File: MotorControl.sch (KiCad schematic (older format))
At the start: 2 parts, among them U3 74LVC125

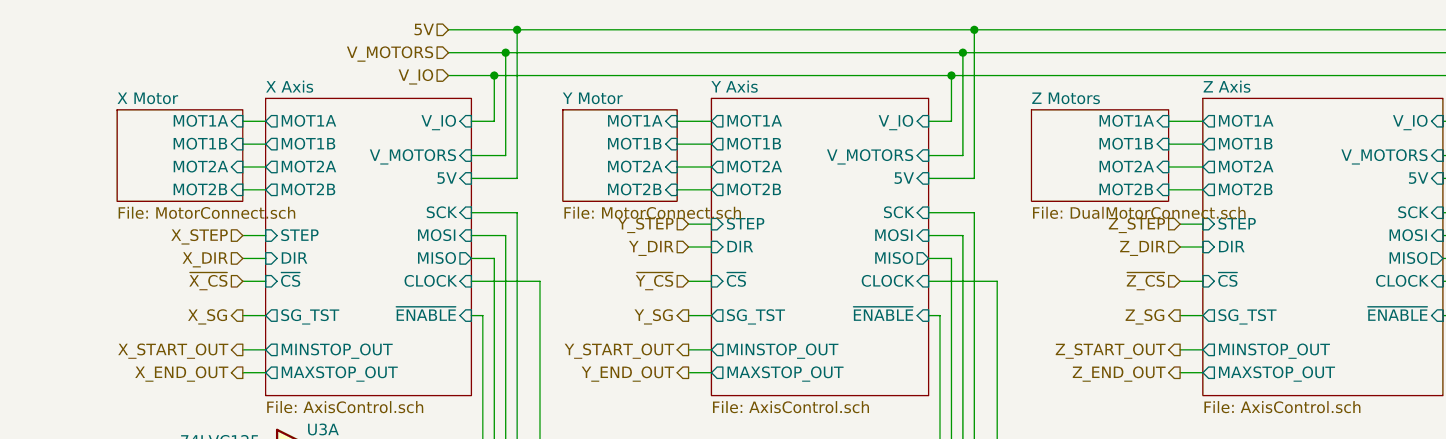
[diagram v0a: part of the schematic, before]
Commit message: Updated motor connector pinout.
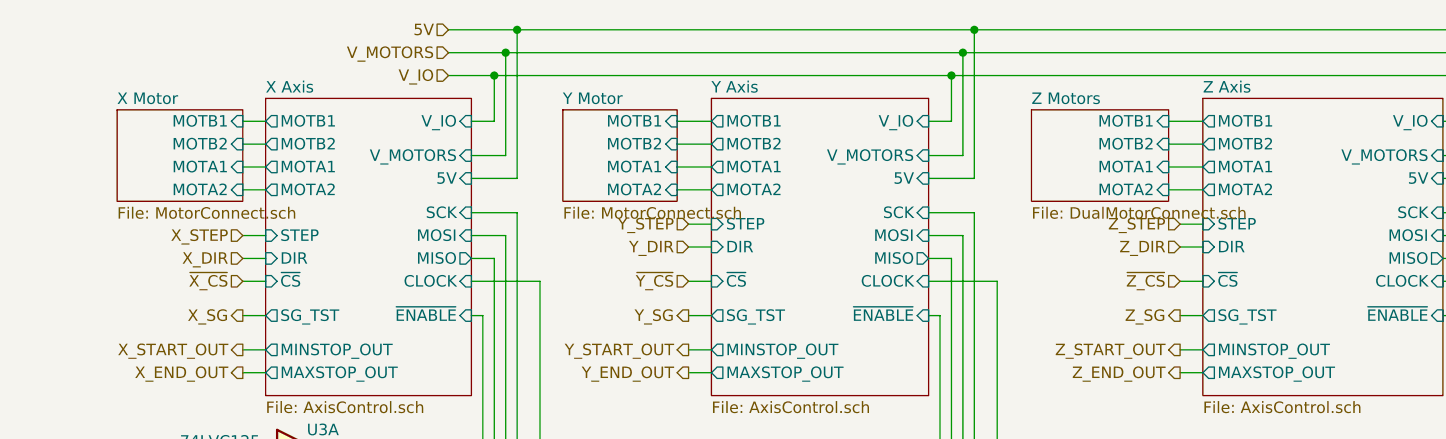
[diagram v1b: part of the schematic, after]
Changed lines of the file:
@@
 F0 "X Axis" 50
 F1 "AxisControl.sch" 50
-F2 "MOT1A" O L 3400 1400 50
-F3 "MOT1B" O L 3400 1500 50
-F4 "MOT2A" O L 3400 1600 50
-F5 "MOT2B" O L 3400 1700 50
-F6 "STEP" I L 3400 1900 50
-F7 "DIR" I L 3400 2000 50
-F8 "~CS" I L 3400 2100 50
-F9 "SG_TST" O L 3400 2250 50
-F10 "V_IO" I R 4300 1400 50
-F11 "V_MOTORS" I R 4300 1550 50
-F12 "SCK" I R 4300 1800 50
-F13 "MOSI" I R 4300 1900 50
-F14 "MISO" O R 4300 2000 50
-F15 "~ENABLE" I R 4300 2250 50
-F16 "MAXSTOP_OUT" O L 3400 2500 50
-F17 "MINSTOP_OUT" O L 3400 2400 50
-F18 "5V" I R 4300 1650 50
-F19 "CLOCK" I R 4300 2100 50
+F2 "STEP" I L 3400 1900 50
+F3 "DIR" I L 3400 2000 50
+F4 "~CS" I L 3400 2100 50
+F5 "SG_TST" O L 3400 2250 50
+F6 "V_IO" I R 4300 1400 50
+F7 "V_MOTORS" I R 4300 1550 50
+F8 "SCK" I R 4300 1800 50
+F9 "MOSI" I R 4300 1900 50
+F10 "MISO" O R 4300 2000 50
+F11 "~ENABLE" I R 4300 2250 50
+F12 "MAXSTOP_OUT" O L 3400 2500 50
+F13 "MINSTOP_OUT" O L 3400 2400 50
+F14 "5V" I R 4300 1650 50
+F15 "CLOCK" I R 4300 2100 50
+F16 "MOTA1" O L 3400 1600 50
+F17 "MOTB1" O L 3400 1400 50
+F18 "MOTA2" O L 3400 1700 50
+F19 "MOTB2" O L 3400 1500 50
 $EndSheet
 $Sheet
@@
 F0 "Y Axis" 50
 F1 "AxisControl.sch" 50
-F2 "MOT1A" O L 5350 1400 50
-F3 "MOT1B" O L 5350 1500 50
-F4 "MOT2A" O L 5350 1600 50
-F5 "MOT2B" O L 5350 1700 50
-F6 "STEP" I L 5350 1850 50
-F7 "DIR" I L 5350 1950 50
-F8 "~CS" I L 5350 2100 50
-F9 "SG_TST" O L 5350 2250 50
-F10 "V_IO" I R 6300 1400 50
-F11 "V_MOTORS" I R 6300 1550 50
-F12 "SCK" I R 6300 1800 50
-F13 "MOSI" I R 6300 1900 50
-F14 "MISO" O R 6300 2000 50
-F15 "~ENABLE" I R 6300 2250 50
-F16 "MAXSTOP_OUT" O L 5350 2500 50
-F17 "MINSTOP_OUT" O L 5350 2400 50
-F18 "5V" I R 6300 1650 50
-F19 "CLOCK" I R 6300 2100 50
+F2 "STEP" I L 5350 1850 50
+F3 "DIR" I L 5350 1950 50
+F4 "~CS" I L 5350 2100 50
+F5 "SG_TST" O L 5350 2250 50
+F6 "V_IO" I R 6300 1400 50
+F7 "V_MOTORS" I R 6300 1550 50
+F8 "SCK" I R 6300 1800 50
+F9 "MOSI" I R 6300 1900 50
+F10 "MISO" O R 6300 2000 50
+F11 "~ENABLE" I R 6300 2250 50
+F12 "MAXSTOP_OUT" O L 5350 2500 50
+F13 "MINSTOP_OUT" O L 5350 2400 50
+F14 "5V" I R 6300 1650 50
+F15 "CLOCK" I R 6300 2100 50
+F16 "MOTA1" O L 5350 1600 50
+F17 "MOTB1" O L 5350 1400 50
+F18 "MOTA2" O L 5350 1700 50
+F19 "MOTB2" O L 5350 1500 50
 $EndSheet
 Wire Wire Line
@@
 F0 "Z Axis" 50
 F1 "AxisControl.sch" 50
-F2 "MOT1A" O L 7500 1400 50
-F3 "MOT1B" O L 7500 1500 50
-F4 "MOT2A" O L 7500 1600 50
-F5 "MOT2B" O L 7500 1700 50
-F6 "STEP" I L 7500 1850 50
-F7 "DIR" I L 7500 1950 50
-F8 "~CS" I L 7500 2100 50
-F9 "SG_TST" O L 7500 2250 50
-F10 "V_IO" I R 8550 1400 50
-F11 "V_MOTORS" I R 8550 1550 50
-F12 "SCK" I R 8550 1800 50
-F13 "MOSI" I R 8550 1900 50
-F14 "MISO" O R 8550 2000 50
-F15 "~ENABLE" I R 8550 2250 50
-F16 "MAXSTOP_OUT" O L 7500 2500 50
-F17 "MINSTOP_OUT" O L 7500 2400 50
-F18 "5V" I R 8550 1650 50
-F19 "CLOCK" I R 8550 2100 50
+F2 "STEP" I L 7500 1850 50
+F3 "DIR" I L 7500 1950 50
+F4 "~CS" I L 7500 2100 50
+F5 "SG_TST" O L 7500 2250 50
+F6 "V_IO" I R 8550 1400 50
+F7 "V_MOTORS" I R 8550 1550 50
+F8 "SCK" I R 8550 1800 50
+F9 "MOSI" I R 8550 1900 50
+F10 "MISO" O R 8550 2000 50
+F11 "~ENABLE" I R 8550 2250 50
+F12 "MAXSTOP_OUT" O L 7500 2500 50
+F13 "MINSTOP_OUT" O L 7500 2400 50
+F14 "5V" I R 8550 1650 50
+F15 "CLOCK" I R 8550 2100 50
+F16 "MOTA1" O L 7500 1600 50
+F17 "MOTB1" O L 7500 1400 50
+F18 "MOTA2" O L 7500 1700 50
+F19 "MOTB2" O L 7500 1500 50
 $EndSheet
 Wire Wire Line
@@
 F0 "X Motor" 50
 F1 "MotorConnect.sch" 50
-F2 "MOT1B" I R 3300 1500 50
-F3 "MOT1A" I R 3300 1400 50
-F4 "MOT2A" I R 3300 1600 50
-F5 "MOT2B" I R 3300 1700 50
+F2 "MOTB1" I R 3300 1400 50
+F3 "MOTB2" I R 3300 1500 50
+F4 "MOTA2" I R 3300 1700 50
+F5 "MOTA1" I R 3300 1600 50
 $EndSheet
 Wire Wire Line
@@
 F0 "Y Motor" 50
 F1 "MotorConnect.sch" 50
-F2 "MOT1B" I R 5200 1500 50
-F3 "MOT1A" I R 5200 1400 50
-F4 "MOT2A" I R 5200 1600 50
-F5 "MOT2B" I R 5200 1700 50
+F2 "MOTB1" I R 5200 1400 50
+F3 "MOTB2" I R 5200 1500 50
+F4 "MOTA2" I R 5200 1700 50
+F5 "MOTA1" I R 5200 1600 50
 $EndSheet
 Wire Wire Line
@@
 F0 "Z Motors" 50
 F1 "DualMotorConnect.sch" 50
-F2 "MOT1A" I R 7350 1400 50
-F3 "MOT1B" I R 7350 1500 50
-F4 "MOT2A" I R 7350 1600 50
-F5 "MOT2B" I R 7350 1700 50
-$EndSheet
-Wire Wire Line
+F2 "MOTB2" I R 7350 1500 50
+F3 "MOTB1" I R 7350 1400 50
+F4 "MOTA2" I R 7350 1700 50
+F5 "MOTA1" I R 7350 1600 50
+$EndSheet
+Wire Wire Line

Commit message: Some useless changes, I'll remove the SD_MODE wire soon.
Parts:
- added JP10: Motor Clock Enable, Jumper:SolderJumper-2_P1.3mm_Open_Pad1.0x1.5mm, symbol Device:Jumper
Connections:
- net labels added: SD_MODE
- wire segments 203 -> 218
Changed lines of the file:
@@
 F16 "5V" I R 4250 4400 50
 F17 "CLOCK" I R 4250 4850 50
+F18 "SD_MODE" I R 4250 5050 50
 $EndSheet
 $Sheet
@@
 F18 "MOTA2" O L 3400 1700 50
 F19 "MOTB2" O L 3400 1500 50
+F20 "SD_MODE" I R 4300 2350 50
 $EndSheet
 $Sheet
@@
 F18 "MOTA2" O L 5350 1700 50
 F19 "MOTB2" O L 5350 1500 50
+F20 "SD_MODE" I R 6300 2350 50
 $EndSheet
 Wire Wire Line
@@
 F18 "MOTA2" O L 7500 1700 50
 F19 "MOTB2" O L 7500 1500 50
+F20 "SD_MODE" I R 8550 2350 50
 $EndSheet
 Wire Wire Line
@@
 F16 "5V" I R 6450 4400 50
 F17 "CLOCK" I R 6450 4850 50
+F18 "SD_MODE" I R 6450 5050 50
 $EndSheet
 Wire Wire Line
@@
 	8550 2100 8800 2100
 Wire Wire Line
-	8800 2100 8800 3250
-Wire Wire Line
 	8800 3450 7300 3450
 Connection ~ 6600 3450
@@
 Wire Wire Line
 	7300 3450 6600 3450
-Wire Wire Line
-	9800 3250 8800 3250
-Connection ~ 8800 3250
-Wire Wire Line
-	8800 3250 8800 3450
 Text HLabel 10550 3250 2    50   Input ~ 0
 CLOCK
 Wire Wire Line
 	10550 3250 10400 3250
+Wire Wire Line
+	8800 2100 8800 3250
+$Comp
+L Device:Jumper JP10
+U 1 1 5AF71511
+P 9100 3250
+F 0 "JP10" H 9100 3514 50  0000 C CNN
+F 1 "Motor Clock Enable" H 9200 3400 50  0000 C CNN
+F 2 "Jumper:SolderJumper-2_P1.3mm_Open_Pad1.0x1.5mm" H 9100 3250 50  0001 C CNN
+F 3 "~" H 9100 3250 50  0001 C CNN
+	1    9100 3250
+	1    0    0    -1
+$EndComp
+Connection ~ 8800 3250
+Wire Wire Line
+	8800 3250 8800 3450
+Wire Wire Line
+	9400 3250 9800 3250
+Wire Wire Line
+	4300 2350 4650 2350
+Wire Wire Line
+	4650 2350 4650 2800
+Wire Wire Line
+	4650 2800 4800 2800
+Wire Wire Line
+	8850 2800 8850 2350
+Wire Wire Line
+	8850 2350 8550 2350
+Wire Wire Line
+	6300 2350 6800 2350
+Wire Wire Line
+	6800 2350 6800 2800
+Connection ~ 6800 2800
+Wire Wire Line
+	6800 2800 7000 2800
+Wire Wire Line
+	6450 5050 7000 5050
+Wire Wire Line
+	7000 5050 7000 2800
+Connection ~ 7000 2800
+Wire Wire Line
+	7000 2800 8850 2800
+Wire Wire Line
+	4250 5050 4800 5050
+Wire Wire Line
+	4800 5050 4800 2800
+Connection ~ 4800 2800
+Wire Wire Line
+	4800 2800 6800 2800
+Text HLabel 10550 2800 2    50   Input ~ 0
+SD_MODE
+Wire Wire Line
+	8850 2800 10550 2800
+Connection ~ 8850 2800
 $EndSCHEMATC

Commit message: Removed SD_MODE wire. Added motor clock oscillator. Wired the clock on the internal layer to reduce EMI.
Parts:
- removed JP10: Motor Clock Enable, Jumper:SolderJumper-2_P1.3mm_Open_Pad1.0x1.5mm, symbol Device:Jumper
- added C90: 0.1uF, Capacitor_SMD:C_0603_1608Metric, symbol Device:C
- added X1: 16MHz, Oscillator:Oscillator_SMD_EuroQuartz_XO32-4Pin_3.2x2.5mm_HandSoldering, symbol Oscillator:XO32
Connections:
- net labels removed: CLOCK, SD_MODE
- wire segments 218 -> 215
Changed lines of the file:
@@
 F16 "5V" I R 4250 4400 50
 F17 "CLOCK" I R 4250 4850 50
-F18 "SD_MODE" I R 4250 5050 50
 $EndSheet
 $Sheet
@@
 F18 "MOTA2" O L 3400 1700 50
 F19 "MOTB2" O L 3400 1500 50
-F20 "SD_MODE" I R 4300 2350 50
 $EndSheet
 $Sheet
@@
 F18 "MOTA2" O L 5350 1700 50
 F19 "MOTB2" O L 5350 1500 50
-F20 "SD_MODE" I R 6300 2350 50
 $EndSheet
 Wire Wire Line
@@
 F18 "MOTA2" O L 7500 1700 50
 F19 "MOTB2" O L 7500 1500 50
-F20 "SD_MODE" I R 8550 2350 50
 $EndSheet
 Wire Wire Line
@@
 F16 "5V" I R 6450 4400 50
 F17 "CLOCK" I R 6450 4850 50
-F18 "SD_MODE" I R 6450 5050 50
 $EndSheet
 Wire Wire Line
@@
 Wire Wire Line
 	7300 3450 6600 3450
-Text HLabel 10550 3250 2    50   Input ~ 0
-CLOCK
-Wire Wire Line
-	10550 3250 10400 3250
 Wire Wire Line
 	8800 2100 8800 3250
-$Comp
-L Device:Jumper JP10
-U 1 1 5AF71511
-P 9100 3250
-F 0 "JP10" H 9100 3514 50  0000 C CNN
-F 1 "Motor Clock Enable" H 9200 3400 50  0000 C CNN
-F 2 "Jumper:SolderJumper-2_P1.3mm_Open_Pad1.0x1.5mm" H 9100 3250 50  0001 C CNN
-F 3 "~" H 9100 3250 50  0001 C CNN
-	1    9100 3250
-	1    0    0    -1
-$EndComp
+Wire Wire Line
+	8800 3250 9800 3250
 Connection ~ 8800 3250
 Wire Wire Line
 	8800 3250 8800 3450
-Wire Wire Line
-	9400 3250 9800 3250
-Wire Wire Line
-	4300 2350 4650 2350
-Wire Wire Line
-	4650 2350 4650 2800
-Wire Wire Line
-	4650 2800 4800 2800
-Wire Wire Line
-	8850 2800 8850 2350
-Wire Wire Line
-	8850 2350 8550 2350
-Wire Wire Line
-	6300 2350 6800 2350
-Wire Wire Line
-	6800 2350 6800 2800
-Connection ~ 6800 2800
-Wire Wire Line
-	6800 2800 7000 2800
-Wire Wire Line
-	6450 5050 7000 5050
-Wire Wire Line
-	7000 5050 7000 2800
-Connection ~ 7000 2800
-Wire Wire Line
-	7000 2800 8850 2800
-Wire Wire Line
-	4250 5050 4800 5050
-Wire Wire Line
-	4800 5050 4800 2800
-Connection ~ 4800 2800
-Wire Wire Line
-	4800 2800 6800 2800
-Text HLabel 10550 2800 2    50   Input ~ 0
-SD_MODE
-Wire Wire Line
-	8850 2800 10550 2800
-Connection ~ 8850 2800
+$Comp
+L Oscillator:XO32 X1
+U 1 1 5AFB04B7
+P 10050 4450
+F 0 "X1" H 10391 4496 50  0000 L CNN
+F 1 "16MHz" H 10391 4405 50  0000 L CNN
+F 2 "Oscillator:Oscillator_SMD_EuroQuartz_XO32-4Pin_3.2x2.5mm_HandSoldering" H 10750 4100 50  0001 C CNN
+F 3 "http://cdn-reichelt.de/documents/datenblatt/B400/XO32.pdf" H 9950 4450 50  0001 C CNN
+	1    10050 4450
+	1    0    0    -1
+$EndComp
+Wire Wire Line
+	10350 4450 10700 4450
+Wire Wire Line
+	10700 4450 10700 3250
+Wire Wire Line
+	10400 3250 10700 3250
+Wire Wire Line
+	10050 4750 10050 4950
+Wire Wire Line
+	10050 4950 9450 4950
+Wire Wire Line
+	10050 4150 10050 3750
+$Comp
+L Device:C C90
+U 1 1 5AFD7ED2
+P 9450 4450
+F 0 "C90" H 9565 4496 50  0000 L CNN
+F 1 "0.1uF" H 9565 4405 50  0000 L CNN
+F 2 "Capacitor_SMD:C_0603_1608Metric" H 9488 4300 50  0001 C CNN
+F 3 "~" H 9450 4450 50  0001 C CNN
+	1    9450 4450
+	1    0    0    -1
+$EndComp
+Wire Wire Line
+	9750 4450 9750 3750
+Wire Wire Line
+	8700 3750 9450 3750
+Connection ~ 9750 3750
+Wire Wire Line
+	9750 3750 10050 3750
+Wire Wire Line
+	9450 4300 9450 3750
+Connection ~ 9450 3750
+Wire Wire Line
+	9450 3750 9750 3750
+Wire Wire Line
+	9450 4600 9450 4950
+Connection ~ 9450 4950
+Wire Wire Line
+	9450 4950 8700 4950
 $EndSCHEMATC

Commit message: Updated footprints. Added more board text. Moved TR3 down a bit.
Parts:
- X1: footprint Oscillator:Oscillator_SMD_EuroQuartz_XO32-4Pin_3.2x2.5mm_HandSoldering -> PrntrBoardV1:Oscillator_SMD_EuroQuartz_XO32-4Pin_3.2x2.5mm_HandSoldering
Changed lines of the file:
@@
 F 0 "X1" H 10391 4496 50  0000 L CNN
 F 1 "16MHz" H 10391 4405 50  0000 L CNN
-F 2 "Oscillator:Oscillator_SMD_EuroQuartz_XO32-4Pin_3.2x2.5mm_HandSoldering" H 10750 4100 50  0001 C CNN
+F 2 "PrntrBoardV1:Oscillator_SMD_EuroQuartz_XO32-4Pin_3.2x2.5mm_HandSoldering" H 10750 4100 50  0001 C CNN
 F 3 "http://cdn-reichelt.de/documents/datenblatt/B400/XO32.pdf" H 9950 4450 50  0001 C CNN
 	1    10050 4450

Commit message: Added LCD screen. Updated REDME.
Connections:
- net labels added: MOSI_BUF, SCK_BUF
- wire segments 215 -> 219
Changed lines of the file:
@@
 $Descr A4 11693 8268
 encoding utf-8
-Sheet 2 34
+Sheet 2 35
 Title ""
 Date ""
@@
 Connection ~ 6400 3150
 Wire Wire Line
-	8700 3250 8700 1900
+	8700 3250 8700 3050
 Wire Wire Line
 	8700 1900 8550 1900
 Connection ~ 6450 3250
 Wire Wire Line
-	8750 3350 8750 1800
+	8750 3350 8750 2900
 Wire Wire Line
 	8750 1800 8550 1800
@@
 Wire Wire Line
 	9450 4950 8700 4950
+Text HLabel 8950 3050 2    50   Output ~ 0
+MOSI_BUF
+Text HLabel 8950 2900 2    50   Output ~ 0
+SCK_BUF
+Wire Wire Line
+	8700 3050 8950 3050
+Connection ~ 8700 3050
+Wire Wire Line
+	8700 3050 8700 1900
+Wire Wire Line
+	8950 2900 8750 2900
+Connection ~ 8750 2900
+Wire Wire Line
+	8750 2900 8750 1800
 $EndSCHEMATC

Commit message: Updated schematics with the latest features.
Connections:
- net labels removed: 5V
- wire segments 219 -> 202
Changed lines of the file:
@@
 F14 "ETEMP" O L 3350 4600 50
 F15 "PWM" I L 3350 4700 50
-F16 "5V" I R 4250 4400 50
-F17 "CLOCK" I R 4250 4850 50
+F16 "CLOCK" I R 4250 4850 50
 $EndSheet
 $Sheet
@@
 F12 "MAXSTOP_OUT" O L 3400 2500 50
 F13 "MINSTOP_OUT" O L 3400 2400 50
-F14 "5V" I R 4300 1650 50
-F15 "CLOCK" I R 4300 2100 50
-F16 "MOTA1" O L 3400 1600 50
-F17 "MOTB1" O L 3400 1400 50
-F18 "MOTA2" O L 3400 1700 50
-F19 "MOTB2" O L 3400 1500 50
+F14 "CLOCK" I R 4300 2100 50
+F15 "MOTA1" O L 3400 1600 50
+F16 "MOTB1" O L 3400 1400 50
+F17 "MOTA2" O L 3400 1700 50
+F18 "MOTB2" O L 3400 1500 50
 $EndSheet
 $Sheet
@@
 F12 "MAXSTOP_OUT" O L 5350 2500 50
 F13 "MINSTOP_OUT" O L 5350 2400 50
-F14 "5V" I R 6300 1650 50
-F15 "CLOCK" I R 6300 2100 50
-F16 "MOTA1" O L 5350 1600 50
-F17 "MOTB1" O L 5350 1400 50
-F18 "MOTA2" O L 5350 1700 50
-F19 "MOTB2" O L 5350 1500 50
+F14 "CLOCK" I R 6300 2100 50
+F15 "MOTA1" O L 5350 1600 50
+F16 "MOTB1" O L 5350 1400 50
+F17 "MOTA2" O L 5350 1700 50
+F18 "MOTB2" O L 5350 1500 50
 $EndSheet
 Wire Wire Line
@@
 F12 "MAXSTOP_OUT" O L 7500 2500 50
 F13 "MINSTOP_OUT" O L 7500 2400 50
-F14 "5V" I R 8550 1650 50
-F15 "CLOCK" I R 8550 2100 50
-F16 "MOTA1" O L 7500 1600 50
-F17 "MOTB1" O L 7500 1400 50
-F18 "MOTA2" O L 7500 1700 50
-F19 "MOTB2" O L 7500 1500 50
+F14 "CLOCK" I R 8550 2100 50
+F15 "MOTA1" O L 7500 1600 50
+F16 "MOTB1" O L 7500 1400 50
+F17 "MOTA2" O L 7500 1700 50
+F18 "MOTB2" O L 7500 1500 50
 $EndSheet
 Wire Wire Line
@@
 F14 "ETEMP" O L 5450 4600 50
 F15 "PWM" I L 5450 4700 50
-F16 "5V" I R 6450 4400 50
-F17 "CLOCK" I R 6450 4850 50
+F16 "CLOCK" I R 6450 4850 50
 $EndSheet
 Wire Wire Line
@@
 Wire Wire Line
 	8700 3750 8700 3550
-Text HLabel 4200 1000 0    50   Input ~ 0
-5V
 Wire Wire Line
 	8700 3950 8700 3750
@@
 	4450 3650 4450 4300
 Wire Wire Line
-	4200 1000 4500 1000
-Wire Wire Line
-	9650 1000 9650 3700
-Wire Wire Line
-	9650 3700 6750 3700
-Wire Wire Line
-	4500 3700 4500 4400
-Wire Wire Line
-	4500 4400 4250 4400
-Wire Wire Line
-	6450 4400 6750 4400
-Wire Wire Line
-	6750 4400 6750 3700
-Connection ~ 6750 3700
-Wire Wire Line
-	6750 3700 4500 3700
-Wire Wire Line
-	8550 1650 8750 1650
-Wire Wire Line
-	8750 1650 8750 1000
-Connection ~ 8750 1000
-Wire Wire Line
-	8750 1000 9650 1000
-Wire Wire Line
-	6300 1650 6500 1650
-Wire Wire Line
-	6500 1650 6500 1000
-Connection ~ 6500 1000
-Wire Wire Line
-	6500 1000 8750 1000
-Wire Wire Line
-	4300 1650 4500 1650
-Wire Wire Line
-	4500 1650 4500 1000
-Connection ~ 4500 1000
-Wire Wire Line
-	4500 1000 6500 1000
-Wire Wire Line
 	4350 3150 4400 3150
 Connection ~ 4400 3150
@@
 Wire Wire Line
 	7300 3450 6600 3450
-Wire Wire Line
-	8800 2100 8800 3250
-Wire Wire Line
-	8800 3250 9800 3250
-Connection ~ 8800 3250
-Wire Wire Line
-	8800 3250 8800 3450
 $Comp
 L Oscillator:XO32 X1
@@
 Wire Wire Line
 	8750 2900 8750 1800
+Wire Wire Line
+	8800 2100 8800 3250
+Wire Wire Line
+	9800 3250 8800 3250
+Connection ~ 8800 3250
+Wire Wire Line
+	8800 3250 8800 3450
 $EndSCHEMATC

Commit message: Cleanup paths and library names.
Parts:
- U3: symbol Logic_74xx:74LVC125 -> 74ls125:74LVC125
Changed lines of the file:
@@
 	5450 4000 5350 4000
 $Comp
-L Logic_74xx:74LVC125 U3
+L 74ls125:74LVC125 U3
 U 1 1 5ABD1500
 P 3600 2900
@@
 $EndComp
 $Comp
-L Logic_74xx:74LVC125 U3
+L 74ls125:74LVC125 U3
 U 3 1 5ABD166B
 P 2900 3550
@@
 Connection ~ 2900 3800
 $Comp
-L Logic_74xx:74LVC125 U3
+L 74ls125:74LVC125 U3
 U 2 1 5ABD15E4
 P 3250 3200
@@
 	2550 3200 2950 3200
 $Comp
-L Logic_74xx:74LVC125 U3
+L 74ls125:74LVC125 U3
 U 4 1 5AC4CBF3
 P 10100 3250
@@
 Connection ~ 8700 3550
 $Comp
-L Logic_74xx:74LVC125 U3
+L 74ls125:74LVC125 U3
 U 5 1 5AC78AD7
 P 8700 4450

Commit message: Add more filtering caps.
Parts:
- added C81, C82: 1000pF, Capacitor_SMD:C_0603_1608Metric, symbol Device:C
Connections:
- wire segments 202 -> 214
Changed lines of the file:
@@
 	8700 3950 8700 3750
 Wire Wire Line
-	8100 4150 8100 3750
+	8100 4150 8100 4050
 Connection ~ 6950 3000
 Connection ~ 6900 3150
@@
 U 5 1 5AC78AD7
 P 8700 4450
-F 0 "U3" H 8930 4496 50  0000 L CNN
-F 1 "74LVC125" H 8930 4405 50  0000 L CNN
+F 0 "U3" H 8950 4150 50  0000 L CNN
+F 1 "74LVC125" H 8800 4050 50  0000 L CNN
 F 2 "Package_SO:TSSOP-14_4.4x5mm_P0.65mm" H 8700 4450 50  0001 C CNN
 F 3 "http://www.ti.com/lit/gpn/sn74LVC125" H 8700 4450 50  0001 C CNN
@@
 	8100 4950 8700 4950
 Wire Wire Line
-	8100 4450 8100 4950
+	8100 4450 8100 4600
 Wire Wire Line
 	8700 5050 8700 4950
@@
 U 1 1 5AFD7ED2
 P 9450 4450
-F 0 "C90" H 9565 4496 50  0000 L CNN
-F 1 "0.1uF" H 9565 4405 50  0000 L CNN
+F 0 "C90" H 9550 4350 50  0000 L CNN
+F 1 "0.1uF" H 9550 4250 50  0000 L CNN
 F 2 "Capacitor_SMD:C_0603_1608Metric" H 9488 4300 50  0001 C CNN
 F 3 "~" H 9450 4450 50  0001 C CNN
@@
 	9750 3750 10050 3750
 Wire Wire Line
-	9450 4300 9450 3750
+	9450 4300 9450 4050
 Connection ~ 9450 3750
 Wire Wire Line
 	9450 3750 9750 3750
 Wire Wire Line
-	9450 4600 9450 4950
+	9450 4600 9450 4700
 Connection ~ 9450 4950
 Wire Wire Line
@@
 Wire Wire Line
 	8800 3250 8800 3450
+$Comp
+L Device:C C81
+U 1 1 5B400CE8
+P 7750 4300
+F 0 "C81" H 7865 4346 50  0000 L CNN
+F 1 "1000pF" H 7800 4200 50  0000 L CNN
+F 2 "Capacitor_SMD:C_0603_1608Metric" H 7788 4150 50  0001 C CNN
+F 3 "~" H 7750 4300 50  0001 C CNN
+	1    7750 4300
+	1    0    0    -1
+$EndComp
+$Comp
+L Device:C C82
+U 1 1 5B400D4B
+P 9200 4450
+F 0 "C82" H 9250 4350 50  0000 L CNN
+F 1 "1000pF" H 9150 4150 50  0000 L CNN
+F 2 "Capacitor_SMD:C_0603_1608Metric" H 9238 4300 50  0001 C CNN
+F 3 "~" H 9200 4450 50  0001 C CNN
+	1    9200 4450
+	1    0    0    -1
+$EndComp
+Wire Wire Line
+	9200 4300 9200 4050
+Wire Wire Line
+	9200 4050 9450 4050
+Connection ~ 9450 4050
+Wire Wire Line
+	9450 4050 9450 3750
+Wire Wire Line
+	9200 4600 9200 4700
+Wire Wire Line
+	9200 4700 9450 4700
+Connection ~ 9450 4700
+Wire Wire Line
+	9450 4700 9450 4950
+Wire Wire Line
+	7750 4150 7750 4050
+Wire Wire Line
+	7750 4050 8100 4050
+Connection ~ 8100 4050
+Wire Wire Line
+	8100 4050 8100 3750
+Wire Wire Line
+	7750 4450 7750 4600
+Wire Wire Line
+	7750 4600 8100 4600
+Connection ~ 8100 4600
+Wire Wire Line
+	8100 4600 8100 4950
 $EndSCHEMATC
